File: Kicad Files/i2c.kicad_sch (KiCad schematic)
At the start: 52 parts, among them J1 BATT_1_OLED, J2 BATT_2_OLED, J3 ADIRS_OLED

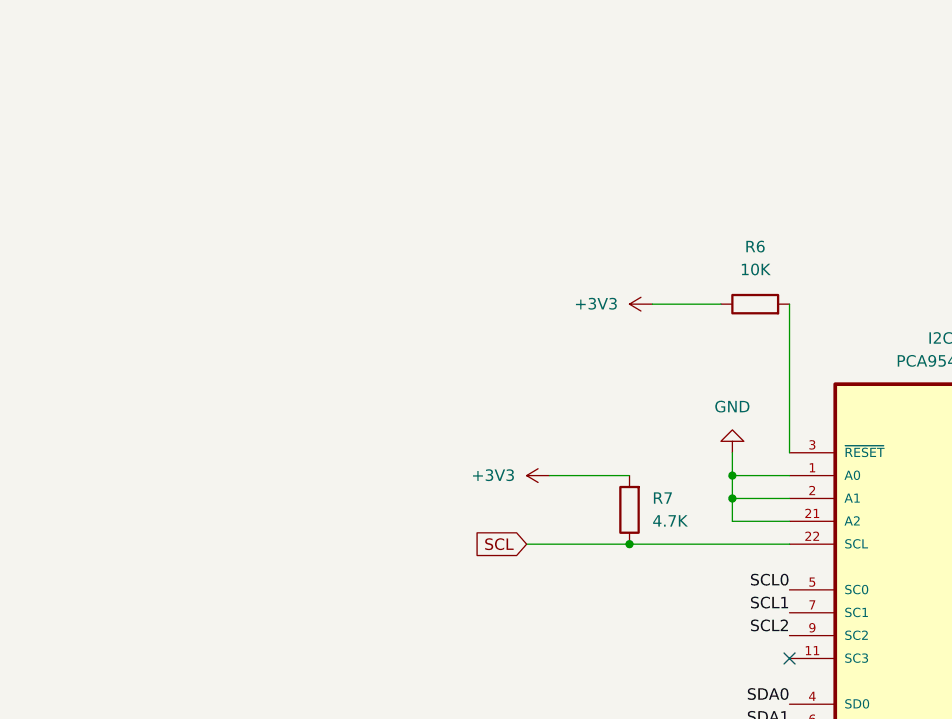
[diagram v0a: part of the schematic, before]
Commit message: Improved pcb design by adding a dip-switch to alter I2C physical address and other small design improvements
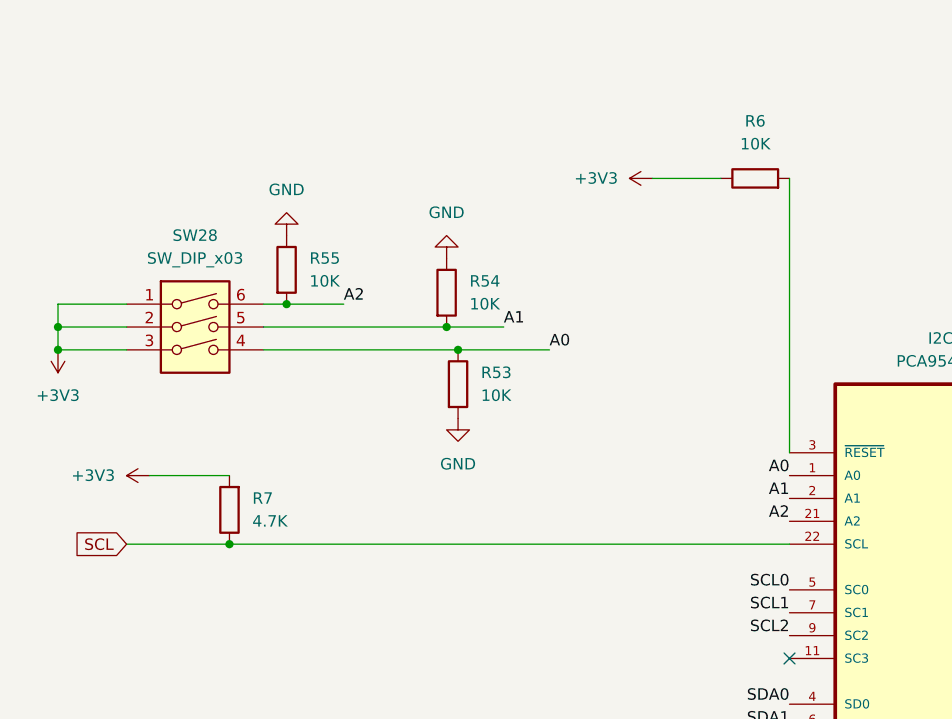
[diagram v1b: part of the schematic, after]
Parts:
- added R53, R54, R55: 10K, Resistor_SMD:R_1206_3216Metric_Pad1.30x1.75mm_HandSolder, symbol Device:R
- added SW28: SW_DIP_x03, Button_Switch_THT:SW_DIP_SPSTx03_Slide_9.78x9.8mm_W7.62mm_P2.54mm, symbol Switch:SW_DIP_x03
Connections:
- net +3V3: now also SW28.1, SW28.2, SW28.3
- net GND: now also R53.2, R54.1, R55.1; no longer I2C_1.1 (A0), I2C_1.2 (A1), I2C_1.21 (A2)
- new net A0: I2C_1.1 (A0), R53.1, SW28.4
- new net A1: I2C_1.2 (A1), R54.2, SW28.5
- new net A2: I2C_1.21 (A2), R55.2, SW28.6
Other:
- moved on the sheet: R6, R7

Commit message: New STL files for APU OVHD element, other coming in the next few weeks
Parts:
- I2C_1: footprint SFLibrary:SOP65P640X120-24N -> PCM_SFLibrary:SOP65P640X120-24N
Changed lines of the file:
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@@
 (kicad_sch
-	(version 20231120)
+	(version 20250114)
 	(generator "eeschema")
-	(generator_version "8.0")
+	(generator_version "9.0")
 	(paper "A4")
 	(junction
@@
 	(label "SCL0"
 		(at 105.41 85.09 180)
-		(fields_autoplaced yes)
 		(effects
 			(font
@@
 	(label "SCL2"
 		(at 105.41 90.17 180)
-		(fields_autoplaced yes)
 		(effects
 			(font
@@
 	(label "SCL1"
 		(at 186.69 130.81 180)
-		(fields_autoplaced yes)
 		(effects
 			(font
@@
 	(label "A1"
 		(at 73.66 55.88 0)
-		(fields_autoplaced yes)
 		(effects
 			(font
@@
 	(label "SDA0"
 		(at 205.74 87.63 270)
-		(fields_autoplaced yes)
 		(effects
 			(font
@@
 	(label "A2"
 		(at 55.88 53.34 0)
-		(fields_autoplaced yes)
 		(effects
 			(font
@@
 	(label "SCL2"
 		(at 198.12 34.29 270)
-		(fields_autoplaced yes)
 		(effects
 			(font
@@
 	(label "SDA2"
 		(at 200.66 34.29 270)
-		(fields_autoplaced yes)
 		(effects
 			(font
@@
 	(label "SCL1"
 		(at 105.41 87.63 180)
-		(fields_autoplaced yes)
 		(effects
 			(font
@@
 	(label "SCL0"
 		(at 203.2 87.63 270)
-		(fields_autoplaced yes)
 		(effects
 			(font
@@
 	(label "A0"
 		(at 78.74 58.42 0)
-		(fields_autoplaced yes)
 		(effects
 			(font
@@
 	(label "A1"
 		(at 105.41 74.93 180)
-		(fields_autoplaced yes)
 		(effects
 			(font
@@
 	(label "SDA2"
 		(at 209.55 139.7 180)
-		(fields_autoplaced yes)
 		(effects
 			(font
@@
 	(label "SDA1"
 		(at 209.55 130.81 180)
-		(fields_autoplaced yes)
 		(effects
 			(font
@@
 	(label "SDA0"
 		(at 209.55 121.92 180)
-		(fields_autoplaced yes)
 		(effects
 			(font
@@
 	(label "SDA1"
 		(at 241.3 87.63 270)
-		(fields_autoplaced yes)
 		(effects
 			(font
@@
 	(label "A0"
 		(at 105.41 72.39 180)
-		(fields_autoplaced yes)
 		(effects
 			(font
@@
 	(label "SCL1"
 		(at 238.76 87.63 270)
-		(fields_autoplaced yes)
 		(effects
 			(font
@@
 	(label "SDA1"
 		(at 105.41 100.33 180)
-		(fields_autoplaced yes)
 		(effects
 			(font
@@
 	(label "SCL0"
 		(at 186.69 121.92 180)
-		(fields_autoplaced yes)
 		(effects
 			(font
@@
 	(label "SCL2"
 		(at 186.69 139.7 180)
-		(fields_autoplaced yes)
 		(effects
 			(font
@@
 	(label "SDA0"
 		(at 105.41 97.79 180)
-		(fields_autoplaced yes)
 		(effects
 			(font
@@
 	(label "A2"
 		(at 105.41 77.47 180)
-		(fields_autoplaced yes)
 		(effects
 			(font
@@
 	(label "SDA2"
 		(at 105.41 102.87 180)
-		(fields_autoplaced yes)
 		(effects
 			(font
@@
 			)
 		)
-		(property "Footprint" "SFLibrary:SOP65P640X120-24N"
+		(property "Footprint" "PCM_SFLibrary:SOP65P640X120-24N"
 			(at 123.19 90.17 0)
 			(effects
